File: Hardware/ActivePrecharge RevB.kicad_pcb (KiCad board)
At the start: 2 copper layers, 98.4 x 58.9 mm, 93 parts, among them IC1 AMC1350DWVR, IC2 AMC1350DWVR, IC3 ZXRE160AET5TA, U1 LT1963AEST-3.3#TRPBF, U2 TLV9001IDBVR, U3 TLV9001IDBVR

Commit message: Fixed this shit finally im free
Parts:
- removed 3V3: 3V3, TestPoint:TestPoint_THTPad_D1.0mm_Drill0.5mm
- removed 3V3, Main, Pre: LED, LED_SMD:LED_0603_1608Metric_Pad1.05x0.95mm_HandSolder
- removed C21: 0.47uF, Capacitor_SMD:C_0603_1608Metric_Pad1.08x0.95mm_HandSolder
- removed C22, C23: 10nF, Capacitor_SMD:C_0603_1608Metric_Pad1.08x0.95mm_HandSolder
- removed Export: ExportConnector, Connector_Molex:Molex_Nano-Fit_105310-xx12_2x06_P2.50mm_Vertical
- removed the G*** at (164.5, 63.0)
- removed the G*** at (177.0, 70.6)
- removed the G*** at (176.5, 63.0)
- removed the G*** at (181.1, 111.8)
- removed the G*** at (144.0, 62.6)
- removed the G*** at (138.0, 62.6)
- removed the G*** at (126.0, 62.6)
- removed the G*** at (108.0, 106.1)
- removed the G*** at (132.0, 62.6)
- removed the HV+ at (116.0, 112.2)
- removed the HV- at (116.0, 108.8)
- removed HVConnector: HVConnector, Connector_Molex:Molex_Nano-Fit_105309-xx03_1x03_P2.50mm_Vertical
- removed the HVGND at (110.0, 112.2)
- removed IC3: ZXRE160AET5TA, ActivePrecharge-RevB:SOT95P280X100-5N
- removed the ISO_5V at (151.0, 67.0)
- removed the ISO_5V at (147.1, 69.0)
- removed LVGND: LVGND, TestPoint:TestPoint_THTPad_D1.0mm_Drill0.5mm
- removed MainCont: MainContactor, Connector_Molex:Molex_Nano-Fit_105309-xx04_1x04_P2.50mm_Vertical
- removed PreCont: PrechargeContactor, Connector_Molex:Molex_Nano-Fit_105309-xx04_1x04_P2.50mm_Vertical
- removed R24, R28, R29: 15k, Resistor_SMD:R_0603_1608Metric_Pad0.98x0.95mm_HandSolder
- removed R25, R30: 10, Resistor_SMD:R_0603_1608Metric_Pad0.98x0.95mm_HandSolder
- removed R26, R27: 2.49k, Resistor_SMD:R_0603_1608Metric_Pad0.98x0.95mm_HandSolder
- removed the REG_3V3 at (142.4, 72.2)
- removed the REG_3V3 at (143.1, 67.0)
- removed U3: TLV9001IDBVR, ActivePrecharge-RevB:DBV0005A_N
- removed V1: V1, TestPoint:TestPoint_THTPad_D1.0mm_Drill0.5mm
- removed V2: V2, TestPoint:TestPoint_THTPad_D1.0mm_Drill0.5mm
- added C18: 1uF, Capacitor_SMD:C_0603_1608Metric_Pad1.08x0.95mm_HandSolder, F.Cu at (156.8, 108.9)
- added C19: 1uF, Capacitor_SMD:C_0603_1608Metric_Pad1.08x0.95mm_HandSolder, F.Cu at (169.8, 107.1)
- added D2: VSSAF522-M3/H, UTSVT-Passives:SODFL5026X125N, F.Cu at (189.5, 81.8)
- added D3: VSSAF522-M3/H, UTSVT-Passives:SODFL5026X125N, F.Cu at (189.0, 113.0)
- added D4: LED, LED_SMD:LED_0603_1608Metric_Pad1.05x0.95mm_HandSolder, F.Cu at (153.0, 81.6)
- added D5: LED, LED_SMD:LED_0603_1608Metric_Pad1.05x0.95mm_HandSolder, F.Cu at (186.1, 84.2)
- added D6: LED, LED_SMD:LED_0603_1608Metric_Pad1.05x0.95mm_HandSolder, F.Cu at (162.0, 82.8)
- added D7: LED, LED_SMD:LED_0603_1608Metric_Pad1.05x0.95mm_HandSolder, F.Cu at (189.7, 118.0)
- added D8: LED, LED_SMD:LED_0603_1608Metric_Pad1.05x0.95mm_HandSolder, F.Cu at (167.1, 81.3)
- added G***: LOGO, LOGO, F.Cu at (181.8, 121.6)
- added G***: LOGO, LOGO, B.Cu at (183.0, 79.0)
- added HV+: Conn_01x01_Pin, Connector_PinHeader_2.54mm:PinHeader_1x01_P2.54mm_Vertical, F.Cu at (136.6, 124.6)
- added HV-: Conn_01x01_Pin, Connector_PinHeader_2.54mm:PinHeader_1x01_P2.54mm_Vertical, F.Cu at (136.6, 74.9)
- added HVGND: HVGND, TestPoint:TestPoint_Keystone_5005-5009_Compact, F.Cu at (117.5, 114.3)
- added ISO_5V: ISO_5V, TestPoint:TestPoint_Keystone_5005-5009_Compact, F.Cu at (160.2, 77.8)
- added J1: HVConnector, Connector_Molex:Molex_Nano-Fit_105309-xx03_1x03_P2.50mm_Vertical, F.Cu at (120.0, 85.1)
- added J2: PrechargeContactor, Connector_Molex:Molex_Nano-Fit_105309-xx04_1x04_P2.50mm_Vertical, F.Cu at (196.4, 81.4)
- added J3: MainContactor, Connector_Molex:Molex_Nano-Fit_105309-xx04_1x04_P2.50mm_Vertical, F.Cu at (196.4, 111.0)
- added J4: ExportConnector, Connector_Molex:Molex_Nano-Fit_105310-xx12_2x06_P2.50mm_Vertical, F.Cu at (193.9, 93.8)
- added J7: Conn_01x02_Pin, Connector_PinHeader_2.54mm:PinHeader_1x02_P2.54mm_Vertical, F.Cu at (174.6, 83.3)
- added R14: 10, Resistor_SMD:R_0603_1608Metric_Pad0.98x0.95mm_HandSolder, F.Cu at (181.7, 107.8)
- added R15: 1k, Resistor_SMD:R_0603_1608Metric_Pad0.98x0.95mm_HandSolder, F.Cu at (154.6, 81.6)
- added R16: 10k, Resistor_SMD:R_0603_1608Metric_Pad0.98x0.95mm_HandSolder, F.Cu at (186.1, 82.6)
- added R17: 1k, Resistor_SMD:R_0603_1608Metric_Pad0.98x0.95mm_HandSolder, F.Cu at (162.0, 84.4)
- added REG_3V3: REG_3V3, TestPoint:TestPoint_Keystone_5005-5009_Compact, F.Cu at (154.0, 77.8)
- added V1+: V+, TestPoint:TestPoint_Keystone_5005-5009_Compact, F.Cu at (178.4, 96.2)
- added V1-: V-, TestPoint:TestPoint_Keystone_5005-5009_Compact, F.Cu at (183.5, 96.2)
- added V2+: V+, TestPoint:TestPoint_Keystone_5005-5009_Compact, F.Cu at (168.5, 120.9)
- added V2-: V-, TestPoint:TestPoint_Keystone_5005-5009_Compact, F.Cu at (174.5, 120.9)
- added VOut1: VOut1, TestPoint:TestPoint_Keystone_5005-5009_Compact, F.Cu at (182.6, 101.8)
- added VOut2: VOut2, TestPoint:TestPoint_Keystone_5005-5009_Compact, F.Cu at (182.6, 113.5)
- C10: value 1nF -> 100nF
- C14: value 1uF -> 100nF
- C17: value 100nF -> 1nF
- C2: value 10uF -> 10nF; footprint Capacitor_SMD:C_0805_2012Metric_Pad1.18x1.45mm_HandSolder -> Capacitor_SMD:C_0603_1608Metric_Pad1.08x0.95mm_HandSolder
- C3: value 1uF -> 10nF
- C4: value 1uF -> 10uF; footprint Capacitor_SMD:C_0603_1608Metric_Pad1.08x0.95mm_HandSolder -> Capacitor_SMD:C_0805_2012Metric_Pad1.18x1.45mm_HandSolder
- C8, C9: value 100nF -> 1uF
- R10, R8: value 100k -> 10k
- R11, R9: value 2.49k -> 10k
- R12, R18, R5, R6, R7: value 1k -> 10k
- R13: value 1k -> 10
- R19: value 5.1k -> 1k
- R20, R22: value 15k -> 100k
- U1: value LT1963AEST-3.3#TRPBF -> TLV9002QDRQ1; footprint ActivePrecharge-RevB:VREG_LT1963AEST-3.3_TRPBF -> Package_SO:SOIC-8_3.9x4.9mm_P1.27mm
- U2: value TLV9001IDBVR -> LT1963AEST-3.3#TRPBF; footprint ActivePrecharge-RevB:DBV0005A_N -> ActivePrecharge-RevB:VREG_LT1963AEST-3.3_TRPBF
- Vin1: value Vin1 -> Vin; footprint TestPoint:TestPoint_THTPad_D1.0mm_Drill0.5mm -> TestPoint:TestPoint_Keystone_5005-5009_Compact
- Vin2: value Vin2 -> Vin; footprint TestPoint:TestPoint_THTPad_D1.0mm_Drill0.5mm -> TestPoint:TestPoint_Keystone_5005-5009_Compact
- moved LOGO2 61.1 mm to (175.1, 74.9)
- moved Vin1 59.0 mm to (161.8, 120.9)
- moved C2 52.0 mm to (185.1, 106.2), turned to 0 degrees
- moved R12 49.8 mm to (173.2, 116.1), turned to 0 degrees
- moved R7 44.3 mm to (173.2, 113.1), turned to 180 degrees
- moved C3 41.8 mm to (185.1, 107.8)
- moved R8 41.7 mm to (173.2, 111.5), turned to 0 degrees
- moved U1 39.6 mm to (175.7, 107.0)
- moved R10 38.7 mm to (173.2, 114.6), turned to 0 degrees
- moved C5 38.7 mm to (179.2, 107.0), turned to 90 degrees
- moved R5 38.7 mm to (173.4, 99.4), turned to 180 degrees
- moved R9 36.5 mm to (173.4, 102.5), turned to 180 degrees
- moved R6 36.2 mm to (173.4, 97.9), turned to 0 degrees
- moved R11 35.1 mm to (173.4, 101.0), turned to 0 degrees
- moved R23 32.1 mm to (154.7, 112.9), turned to 90 degrees
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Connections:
- net Net-(D1-A) renamed /HV+_Fused
- C10 pad 1: /Voltage_Sense/Vin1 -> REG_3V3
- C11 pad 1: /Voltage_Sense/Vin2 -> /Vin1
- C13 pad 1: REG_3V3 -> 3V3
- C13 pad 2: HVGND -> LVGND
- C15 pad 1: 3V3 -> /Vin2
- C15 pad 2: LVGND -> HVGND
- C16 pad 1: 3V3 -> REG_3V3
- C16 pad 2: LVGND -> HVGND
- C17 pad 1: 3V3 -> /Vin2
- C17 pad 2: LVGND -> HVGND
- C2 pad 1: HVGND -> /VOut1
- C2 pad 2: REG_3V3 -> LVGND
- C3 pad 1: 3V3 -> /VOut2
- C4 pad 2: ISO_5V -> REG_3V3
- C6 pad 1: /Voltage_Sense/Vin1 -> 3V3
- C6 pad 2: HVGND -> LVGND
- C7 pad 1: /Voltage_Sense/Vin2 -> 3V3
- C7 pad 2: HVGND -> LVGND
- C8 pad 1: REG_3V3 -> HVGND
- C8 pad 2: HVGND -> ISO_5V
- C9 pad 1: REG_3V3 -> /Vin1
- F1 pad 1: Net-(J1-Pin_1) -> /HV+_PreFuse
- F2 pad 1: Net-(J1-Pin_3) -> /HV-_PreFuse
- F3 pad 2: Net-(J2-Pin_1) -> /3V3_PreFuse
- IC1 pad 2: /Voltage_Sense/Vin1 -> /Vin1
- IC1 pad 6: LVGND -> /V1-
- IC1 pad 7: /Voltage_Sense/V1 -> /V1+
- IC2 pad 2: /Voltage_Sense/Vin2 -> /Vin2
- IC2 pad 6: LVGND -> /V2-
- IC2 pad 7: /Voltage_Sense/V2 -> /V2+
- R10 pad 1: /Voltage_Sense/Vin2 -> /V2-
- R10 pad 2: HV- -> Net-(U1B--)
- R11 pad 1: HVGND -> Net-(R11-Pad1)
- R11 pad 2: /Voltage_Sense/Vin2 -> Net-(U1A--)
- R12 pad 1: /Pre+ -> Net-(U1B--)
- R12 pad 2: Net-(D5-A) -> Net-(R12-Pad2)
- R13 pad 1: /Main+ -> /VOut1
- R13 pad 2: Net-(D6-A) -> Net-(R11-Pad1)
- R18 pad 1: 3V3 -> /Main+
- R18 pad 2: REG_0V8 -> Net-(D7-A)
- R19 pad 1: REG_0V8 -> 3V3
- R19 pad 2: REG_0V8 -> Net-(D8-A)
- R20 pad 1: REG_0V8 -> /Vin1
- R20 pad 2: LVGND -> HV+
- R21 pad 1: REG_0V8 -> HVGND
- R21 pad 2: Net-(U2--) -> /Vin1
- R22 pad 1: Net-(R22-Pad1) -> /Vin2
- R22 pad 2: Net-(U2--) -> HV-
- R23 pad 1: Net-(U2-+) -> HVGND
- R23 pad 2: /Voltage_Sense/V1 -> /Vin2
- R5 pad 1: REG_3V3 -> Net-(U1A-+)
- R5 pad 2: Net-(D2-A) -> /V1+
- R6 pad 1: ISO_5V -> LVGND
- R6 pad 2: Net-(D3-A) -> Net-(U1A-+)
- R7 pad 1: 3V3 -> Net-(U1B-+)
- R7 pad 2: Net-(D4-A) -> /V2+
- R8 pad 1: /Voltage_Sense/Vin1 -> LVGND
- R8 pad 2: HV+ -> Net-(U1B-+)
- R9 pad 1: HVGND -> Net-(U1A--)
- R9 pad 2: /Voltage_Sense/Vin1 -> /V1-
- U1 pad 1: ISO_5V -> Net-(R11-Pad1)
- U1 pad 2: HVGND -> Net-(U1A--)
- U1 pad 3: REG_3V3 -> Net-(U1A-+)
- U1 pad 4: HVGND -> LVGND
- U2 pad 1: Net-(U2-+) -> ISO_5V
- U2 pad 2: Net-(U2--) -> HVGND
- U2 pad 3: 3V3 -> REG_3V3
- U2 pad 4: LVGND -> HVGND
- Vin1 pad 1: /Voltage_Sense/Vin1 -> /Vin1
- Vin2 pad 1: /Voltage_Sense/Vin2 -> /Vin2
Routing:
- net /Voltage_Sense/Vin1: track 38.6 -> 0.00 mm
- net /Voltage_Sense/V1: track 36.7 -> 0.00 mm
- net REG_0V8: track 31.1 -> 0.00 mm, vias 2 -> 0
- net /Vin1: track 0.00 -> 27.9 mm
- net /Voltage_Sense/Vin2: track 26.4 -> 0.00 mm
- net /Voltage_Sense/V2: track 24.2 -> 0.00 mm, vias 2 -> 0
- net REG_3V3: track 24.1 -> 46.8 mm, vias 5 -> 3
- net /Vin2: track 0.00 -> 18.3 mm
- net Net-(R11-Pad1): track 0.00 -> 17.8 mm
- net /V1-: track 0.00 -> 17.8 mm, vias 0 -> 1
- net Net-(J2-Pin_1): track 16.3 -> 0.00 mm
- net HV+: track 38.9 -> 22.8 mm
- net /V1+: track 0.00 -> 14.7 mm
- net Net-(R12-Pad2): track 0.00 -> 14.6 mm
- net Net-(J1-Pin_1): track 14.3 -> 0.00 mm
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- added copper zone on F.Cu, net /HV+_Fused
- added copper zone on F.Cu, net /HV+_PreFuse
- added copper zone on F.Cu, net /HV-_PreFuse
- removed copper zone on B.Cu, net 3V3
- removed copper zone on B.Cu, net REG_3V3
- removed copper zone on F.Cu, net REG_3V3
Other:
- board size 98.4 x 58.9 mm -> 96 x 57 mm
- board text added: "Active Precharge Rev B Gavin Wang December 2025"
- board text added: "M+"
- board text added: "P+"
- board text added: "PS+"
- board text added: "Validated"
- board text removed: ">"
- board text removed: "Gavin Wang October 2025"

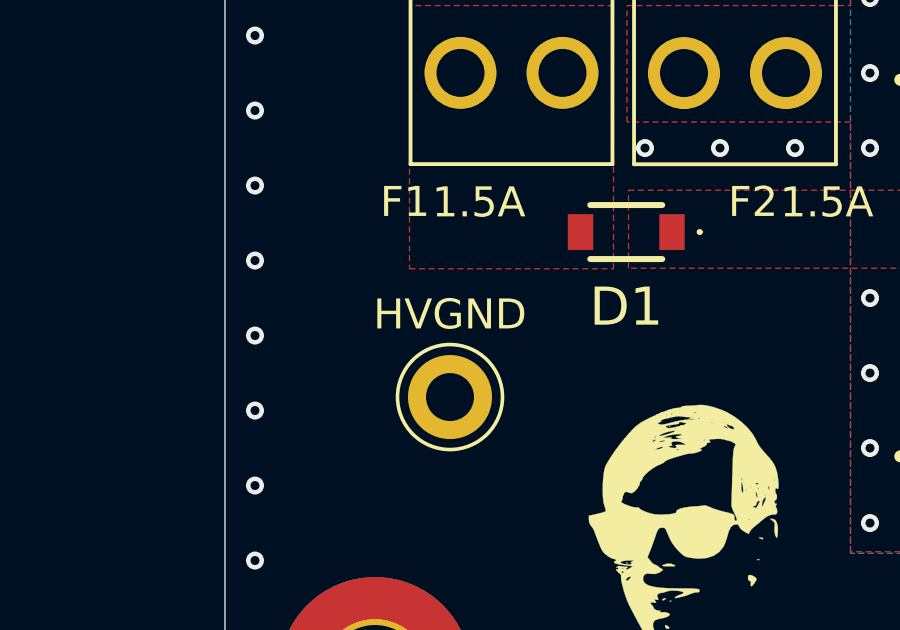
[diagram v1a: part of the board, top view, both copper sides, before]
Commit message: fixed some testpoint silkscreen references i forgot about plus fixed 3d model embedding and added step file
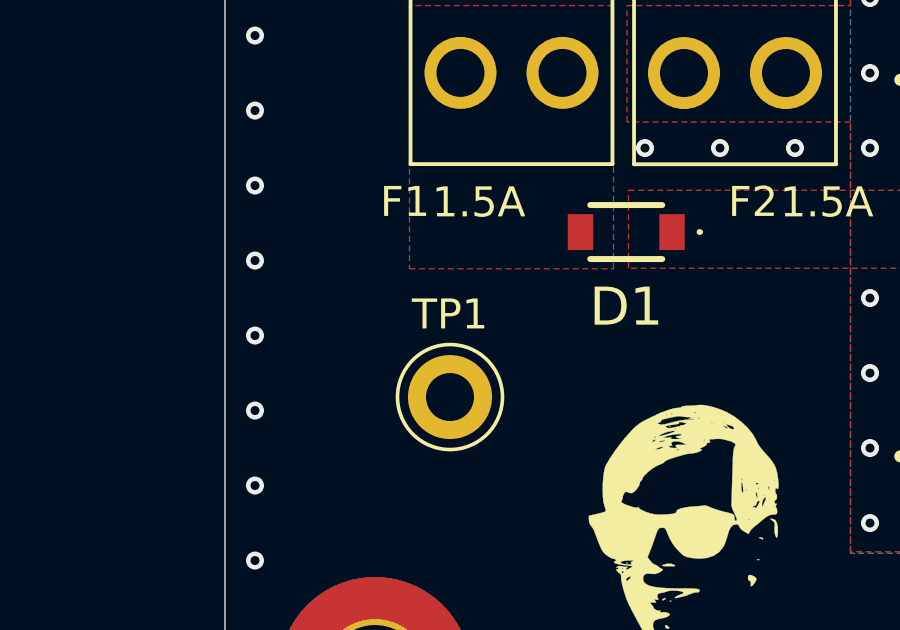
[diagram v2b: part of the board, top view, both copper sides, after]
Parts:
- J5: renamed from HV+; value Conn_01x01_Pin -> HV+
- J6: renamed from HV-; value Conn_01x01_Pin -> HV-
- TP10: renamed from V2+; value V+ -> V2+
- TP11: renamed from V2-; value V- -> V2-
- TP6: renamed from Vin1; value Vin -> Vin1
- TP7: renamed from V1+; value V+ -> V1+
- TP8: renamed from V1-; value V- -> V1-
- TP9: renamed from Vin2; value Vin -> Vin2
- renumbered HVGND to TP1, VOut1 to TP2, VOut2 to TP3, REG_3V3 to TP4, ISO_5V to TP5

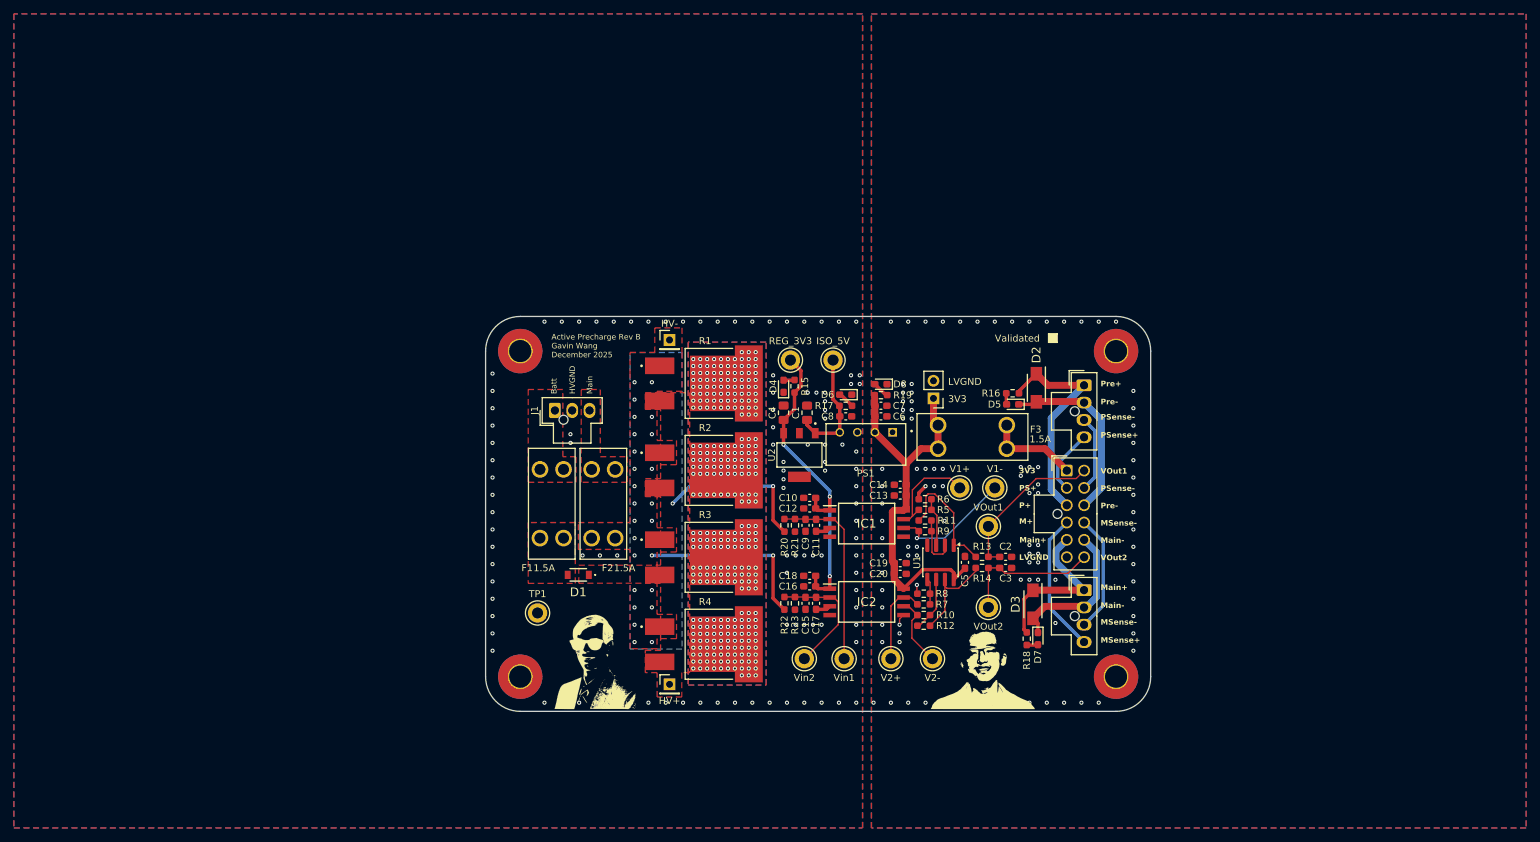
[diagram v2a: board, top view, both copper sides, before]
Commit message: added some silkscreen stuff and gerbers + bom etc
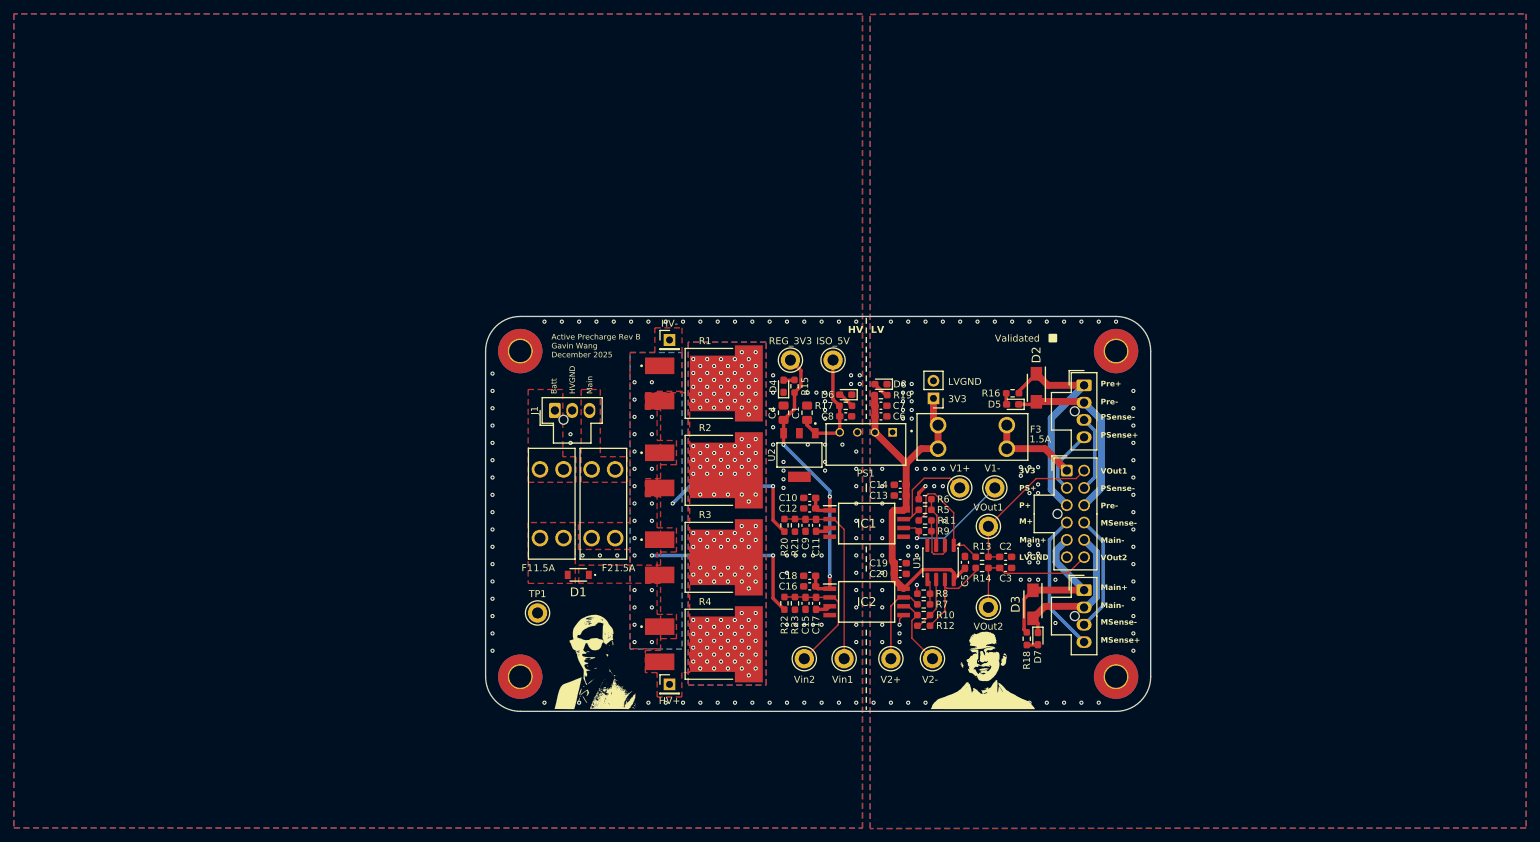
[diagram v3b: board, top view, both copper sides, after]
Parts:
- TP10: value V2+ -> V+
- TP11: value V2- -> V-
- TP6: value Vin1 -> Vin
- TP7: value V1+ -> V+
- TP8: value V1- -> V-
- TP9: value Vin2 -> Vin
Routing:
- net /HEAT_DISSIPATION: vias 304 -> 152
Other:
- board text added: "HV"
- board text added: "LV"
- board text added: "V1+"
- board text added: "V1-"
- board text added: "V2+"
- board text added: "V2-"
- board text added: "Vin1"
- board text added: "Vin2"

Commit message: added some silkscreen stuff
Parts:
- added G***: LOGO, ActivePrecharge-RevB:Rage, B.Cu at (126.0, 115.0)
- added G***: LOGO, ActivePrecharge-RevB:GoblinCurse, B.Cu at (137.0, 115.0)
- added G***: LOGO, ActivePrecharge-RevB:Wooper, B.Cu at (185.5, 122.2)

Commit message: even MORE silkscreen stuff
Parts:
- added G***: LOGO, ActivePrecharge-RevB:Yakub, F.Cu at (341.0, 70.8)
- added G***: LOGO, ActivePrecharge-RevB:Tarantula, B.Cu at (124.7, 78.0)
- added G***: LOGO, ActivePrecharge-RevB:Yakub, B.Cu at (174.8, 110.6)
